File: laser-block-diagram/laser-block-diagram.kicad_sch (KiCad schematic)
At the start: 19 parts

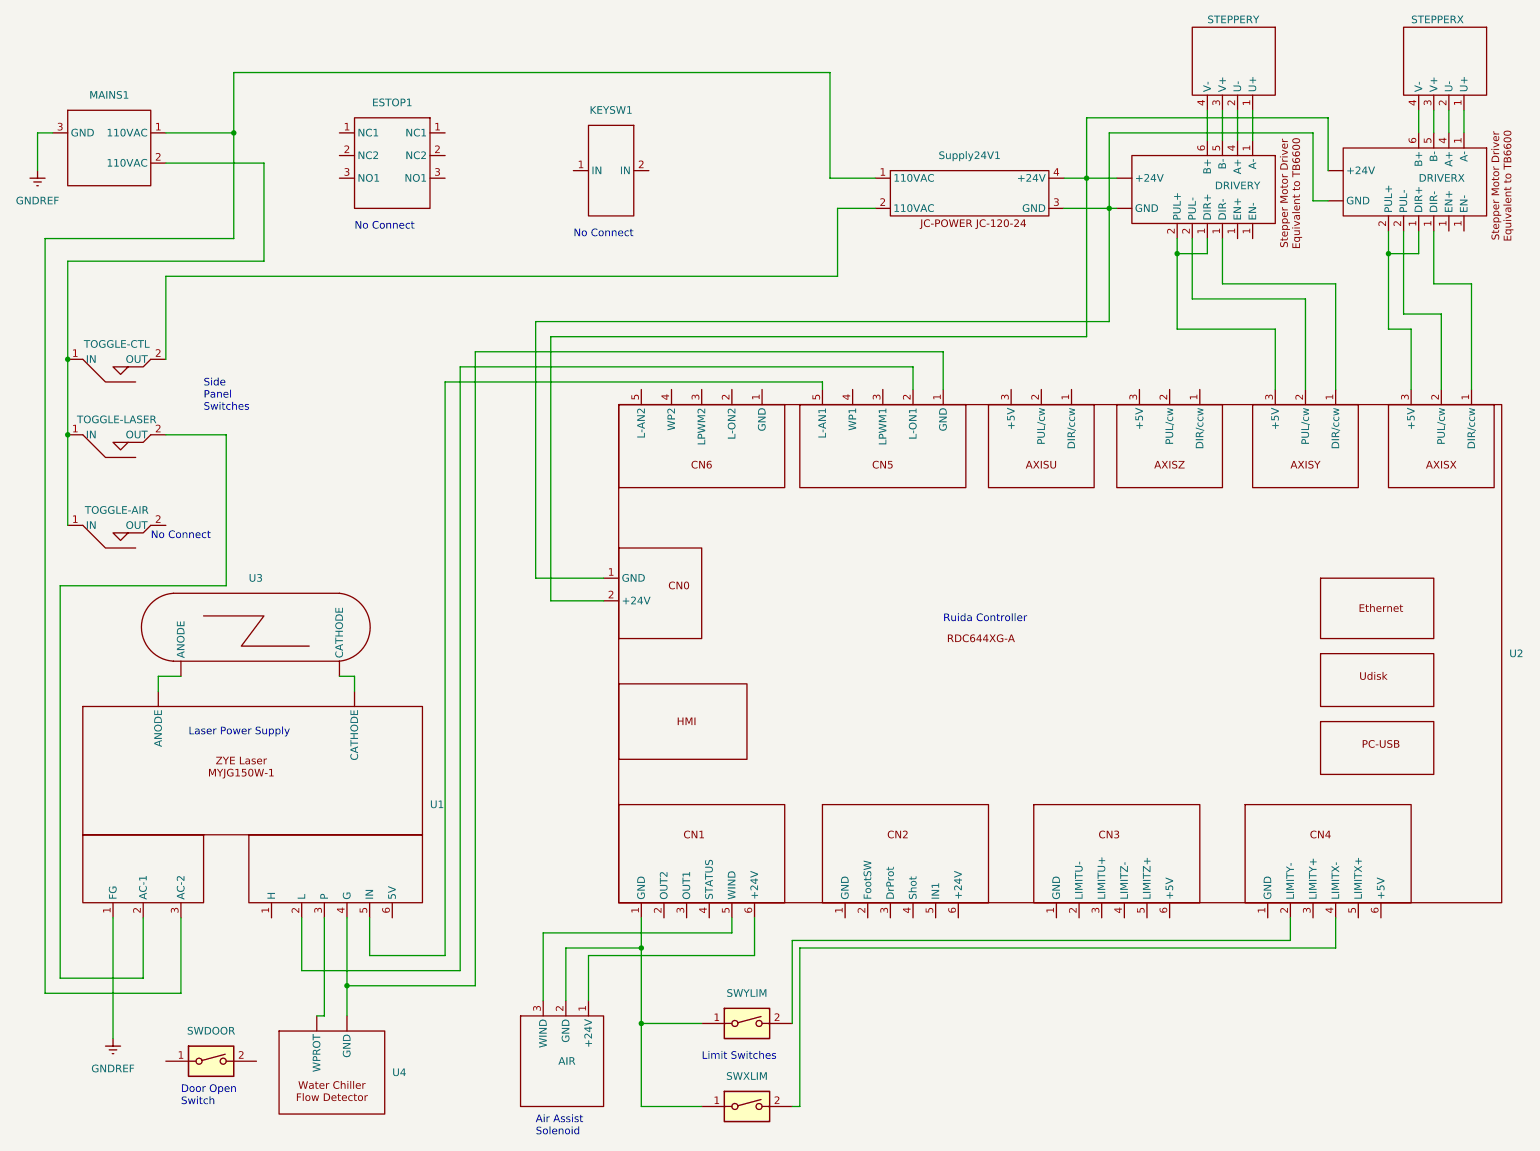
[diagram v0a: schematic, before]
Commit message: Split documents into separate pdfs.
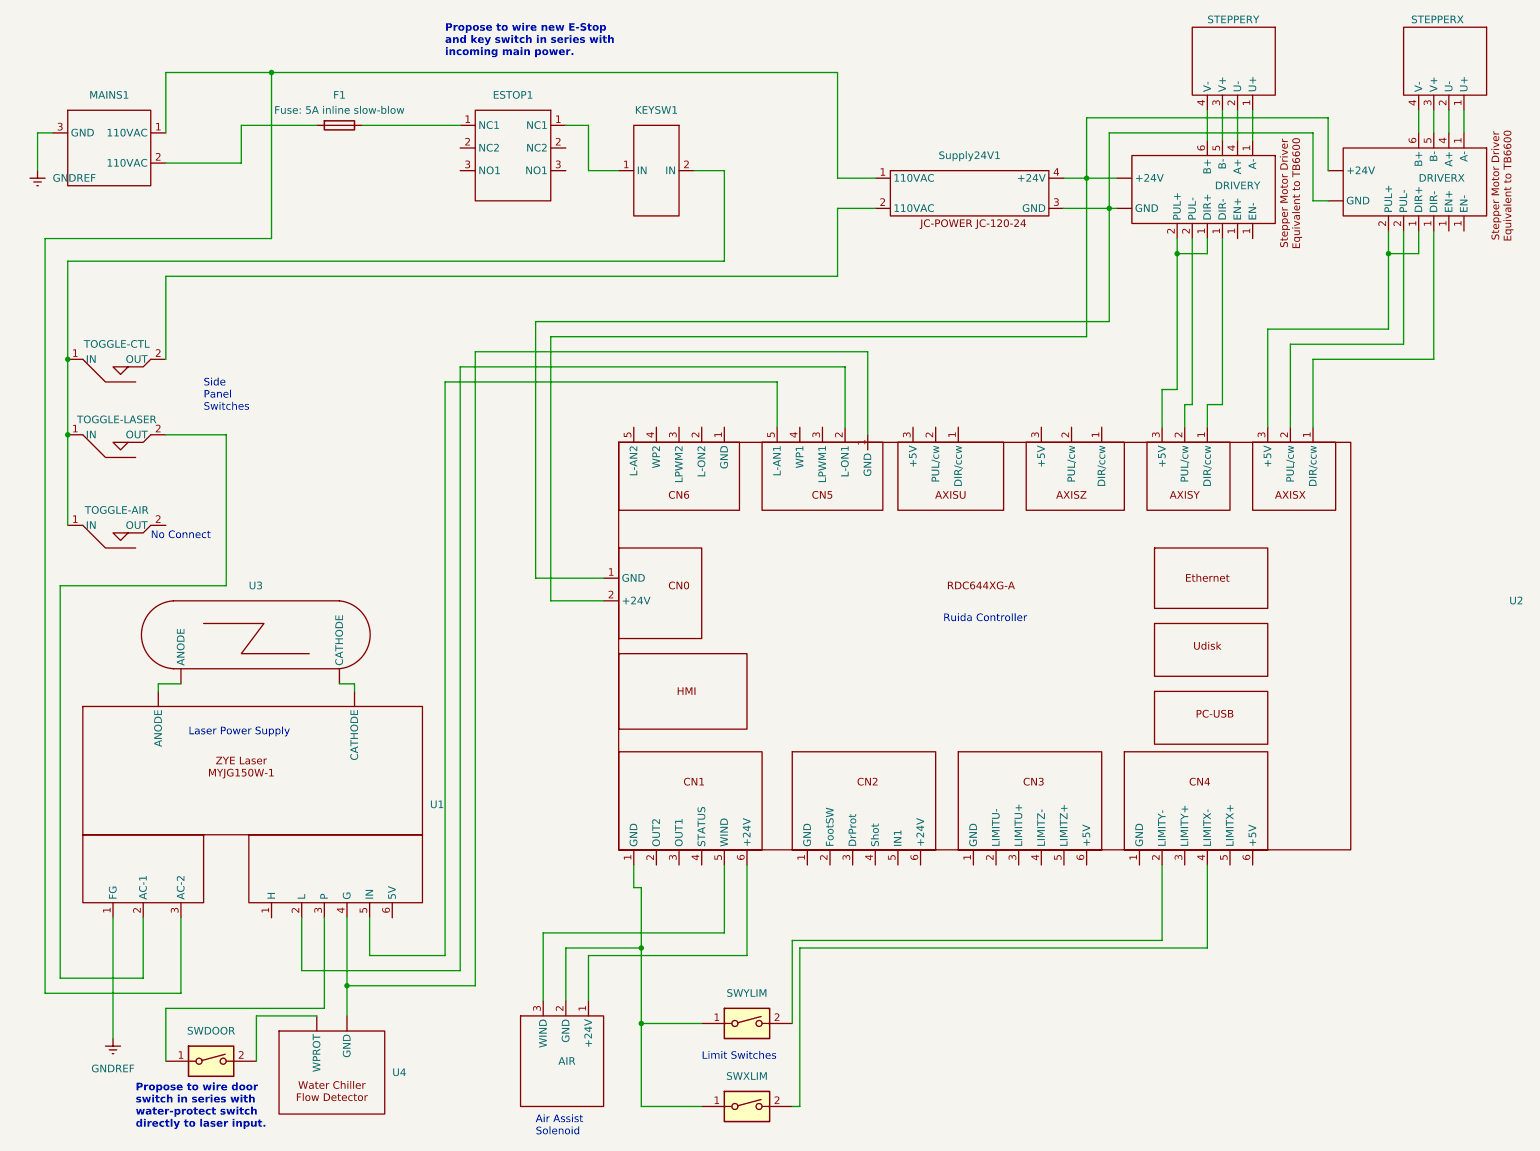
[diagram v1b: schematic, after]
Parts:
- added F1: Fuse: 5A inline slow-blow, symbol Device:Fuse
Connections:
- net at TOGGLE-AIR.1 (IN), TOGGLE-CTL.1 (IN), TOGGLE-LASER.1 (IN): now also KEYSW1.2 (IN); no longer MAINS1.2 (110VAC)
- net at U4. (WPROT): now also SWDOOR.2; no longer U1.3 (P)
- net at U1.2 (L): now also TOGGLE-LASER.2 (OUT); no longer U2.2 (PUL/cw)
- net at U2.1 (GND): now also DRIVERY.1 (EN-)
- net at DRIVERX. (GND), DRIVERY. (GND): now also Supply24V1.4 (+24V), U2.2 (PUL/cw); no longer Supply24V1.3 (GND), U2.1 (GND)
- net at DRIVERX.1 (EN-): no longer U2.1 (GND)
- net at DRIVERY.1 (EN-): no longer U2.1 (GND)
- net at U2.2 (PUL/cw): now also DRIVERY.2 (PUL-)
- net at DRIVERX.2 (PUL-): now also DRIVERX.1 (EN-), U2.3 (OUT1); no longer U2.2 (PUL/cw)
- net at DRIVERY.2 (PUL-): now also DRIVERY.1 (EN-), U2.3 (OUT1); no longer U2.2 (PUL/cw)
- net at SWDOOR.1: now also U1.3 (P)
- net at ESTOP1.1 (NC1): now also KEYSW1.1 (IN)
- new net: U1.4 (G), U2.1 (GND), U4. (WPROT)
- new net: U1. (CATHODE), U3. (CATHODE)
- new net: U1.2 (L), U2.2 (PUL/cw)
- new net: DRIVERX. (GND), DRIVERY. (GND), Supply24V1.3 (GND), U2.1 (GND)
- new net: DRIVERX.1 (EN-), U2.1 (GND)
- new net: DRIVERX.2 (PUL-), U2.2 (PUL/cw)
- new net: ESTOP1.1 (NC1), F1.1
- new net: F1.2, MAINS1.2 (110VAC)
- now unconnected: DRIVERX.1 (EN-), DRIVERY.1 (EN-)
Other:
- note added: "Propose to wire door switch in series with water-protect switch directly to laser input."
- note added: "Propose to wire new E-Stop and key switch in series with incoming main power."
- note removed: "Door Open Switch"
- moved on the sheet: ESTOP1, KEYSW1, U2, U3

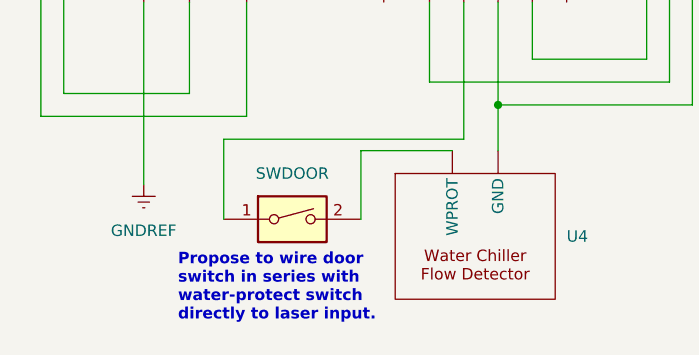
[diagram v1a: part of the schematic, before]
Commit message: Added callibration objects.
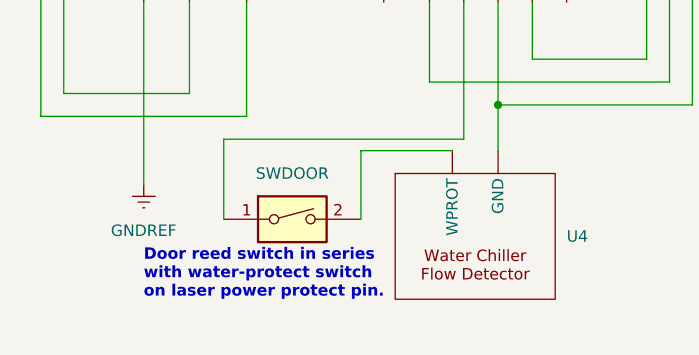
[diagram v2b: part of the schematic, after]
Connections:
- net at U1.2 (L): now also TOGGLE-LASER.2 (OUT); no longer U2.2 (PUL/cw)
- net at U2.1 (GND): now also DRIVERY.1 (EN-)
- net at DRIVERX. (GND), DRIVERY. (GND): now also Supply24V1.4 (+24V), U2.2 (PUL/cw); no longer Supply24V1.3 (GND), U2.1 (GND)
- net at DRIVERX.1 (EN-): no longer U2.1 (GND)
- net at DRIVERY.1 (EN-): no longer U2.1 (GND)
- net at U2.2 (PUL/cw): now also DRIVERY.2 (PUL-)
- net at DRIVERX.2 (PUL-): now also DRIVERX.1 (EN-), U2.3 (OUT1); no longer U2.2 (PUL/cw)
- net at DRIVERY.2 (PUL-): now also DRIVERY.1 (EN-), U2.3 (OUT1); no longer U2.2 (PUL/cw)
- new net: U1.4 (G), U2.1 (GND), U4. (WPROT)
- new net: U1. (CATHODE), U3. (CATHODE)
- new net: U1.2 (L), U2.2 (PUL/cw)
- new net: DRIVERX. (GND), DRIVERY. (GND), Supply24V1.3 (GND), U2.1 (GND)
- new net: DRIVERX.1 (EN-), U2.1 (GND)
- new net: DRIVERX.2 (PUL-), U2.2 (PUL/cw)
- now unconnected: DRIVERX.1 (EN-), DRIVERY.1 (EN-)
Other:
- note added: "Door reed switch in series with water-protect switch on laser power protect pin."
- note removed: "Propose to wire door switch in series with water-protect switch directly to laser input."
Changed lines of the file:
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@@
     (effects (font (size 1.27 1.27)) (justify left bottom))
   )
-  (text "Propose to wire door\nswitch in series with\nwater-protect switch\ndirectly to laser input."
-    (at 30.48 200.66 0)
+  (text "Door reed switch in series\nwith water-protect switch\non laser power protect pin."
+    (at 26.67 198.12 0)
     (effects (font (size 1.27 1.27) (thickness 0.254) bold (color 142 2 0 1)) (justify left bottom))
   )
@@
     (pin "4")
     (instances
-      (project "laser-block-diagram-desired"
+      (project "laser-block-diagram"
         (path "/519677db-cee6-463c-9dec-b4142abca24a"
           (reference "STEPPERY") (unit 1)
@@
     (pin "1")
     (instances
-      (project "laser-block-diagram-desired"
+      (project "laser-block-diagram"
         (path "/519677db-cee6-463c-9dec-b4142abca24a"
           (reference "TOGGLE-CTL") (unit 1)
@@
     (pin "")
     (instances
-      (project "laser-block-diagram-desired"
+      (project "laser-block-diagram"
         (path "/519677db-cee6-463c-9dec-b4142abca24a"
           (reference "U4") (unit 1)
@@
     (pin "1")
     (instances
-      (project "laser-block-diagram-desired"
+      (project "laser-block-diagram"
         (path "/519677db-cee6-463c-9dec-b4142abca24a"
           (reference "AIR") (unit 1)
@@
     (pin "1")
     (instances
-      (project "laser-block-diagram-desired"
+      (project "laser-block-diagram"
         (path "/519677db-cee6-463c-9dec-b4142abca24a"
           (reference "#PWR01") (unit 1)
@@
     (pin "2")
     (instances
-      (project "laser-block-diagram-desired"
+      (project "laser-block-diagram"
         (path "/519677db-cee6-463c-9dec-b4142abca24a"
           (reference "SWXLIM") (unit 1)
@@
     (pin "")
     (instances
-      (project "laser-block-diagram-desired"
+      (project "laser-block-diagram"
         (path "/519677db-cee6-463c-9dec-b4142abca24a"
           (reference "U1") (unit 1)
@@
     (pin "1")
     (instances
-      (project "laser-block-diagram-desired"
+      (project "laser-block-diagram"
         (path "/519677db-cee6-463c-9dec-b4142abca24a"
           (reference "STEPPERX") (unit 1)
@@
     (pin "2")
     (instances
-      (project "laser-block-diagram-desired"
+      (project "laser-block-diagram"
         (path "/519677db-cee6-463c-9dec-b4142abca24a"
           (reference "U2") (unit 1)
@@
     (pin "1")
     (instances
-      (project "laser-block-diagram-desired"
+      (project "laser-block-diagram"
         (path "/519677db-cee6-463c-9dec-b4142abca24a"
           (reference "Supply24V1") (unit 1)
@@
     (pin "1")
     (instances
-      (project "laser-block-diagram-desired"
+      (project "laser-block-diagram"
         (path "/519677db-cee6-463c-9dec-b4142abca24a"
           (reference "SWYLIM") (unit 1)
@@
     (pin "1")
     (instances
-      (project "laser-block-diagram-desired"
+      (project "laser-block-diagram"
         (path "/519677db-cee6-463c-9dec-b4142abca24a"
           (reference "TOGGLE-LASER") (unit 1)
@@
     (pin "1")
     (instances
-      (project "laser-block-diagram-desired"
+      (project "laser-block-diagram"
         (path "/519677db-cee6-463c-9dec-b4142abca24a"
           (reference "DRIVERX") (unit 1)
@@
     (pin "2")
     (instances
-      (project "laser-block-diagram-desired"
+      (project "laser-block-diagram"
         (path "/519677db-cee6-463c-9dec-b4142abca24a"
           (reference "F1") (unit 1)
@@
     (pin "3")
     (instances
-      (project "laser-block-diagram-desired"
+      (project "laser-block-diagram"
         (path "/519677db-cee6-463c-9dec-b4142abca24a"
           (reference "MAINS1") (unit 1)
@@
     (pin "1")
     (instances
-      (project "laser-block-diagram-desired"
+      (project "laser-block-diagram"
         (path "/519677db-cee6-463c-9dec-b4142abca24a"
           (reference "TOGGLE-AIR") (unit 1)
@@
     (pin "2")
     (instances
-      (project "laser-block-diagram-desired"
+      (project "laser-block-diagram"
         (path "/519677db-cee6-463c-9dec-b4142abca24a"
           (reference "DRIVERY") (unit 1)
@@
     (pin "1")
     (instances
-      (project "laser-block-diagram-desired"
+      (project "laser-block-diagram"
         (path "/519677db-cee6-463c-9dec-b4142abca24a"
           (reference "#PWR03") (unit 1)
@@
     (pin "1")
     (instances
-      (project "laser-block-diagram-desired"
+      (project "laser-block-diagram"
         (path "/519677db-cee6-463c-9dec-b4142abca24a"
           (reference "SWDOOR") (unit 1)
@@
     (pin "1")
     (instances
-      (project "laser-block-diagram-desired"
+      (project "laser-block-diagram"
         (path "/519677db-cee6-463c-9dec-b4142abca24a"
           (reference "ESTOP1") (unit 1)
@@
     (pin "2")
     (instances
-      (project "laser-block-diagram-desired"
+      (project "laser-block-diagram"
         (path "/519677db-cee6-463c-9dec-b4142abca24a"
           (reference "KEYSW1") (unit 1)
@@
     (pin "")
     (instances
-      (project "laser-block-diagram-desired"
+      (project "laser-block-diagram"
         (path "/519677db-cee6-463c-9dec-b4142abca24a"
           (reference "U3") (unit 1)
